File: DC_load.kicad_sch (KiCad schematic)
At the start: 21 parts, among them J2 4 mm terminal, J3 4 mm terminal, J4 4 mm terminal, J5 4 mm terminal, Q1 NPN, Q2 PNP, Q3 IRF3205, Q4 IRF3205, Q5 IRF3205, Q6 IRF3205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

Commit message: New dimensions.
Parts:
- removed D1, D2: 1N4148W, Diode_SMD:D_SOD-123, symbol Diode:1N4148W
- removed HS1: Heatsink, DC_load:AMD_heatsink, symbol Mechanical:Heatsink
- removed J3: 4 mm terminal, DC_load:4mm_terminal_red, symbol Connector:Screw_Terminal_01x01
- removed J4: 4 mm terminal, DC_load:4mm_terminal_black, symbol Connector:Screw_Terminal_01x01
- removed Q1: NPN, symbol Simulation_SPICE:NPN
- removed Q2: PNP, symbol Simulation_SPICE:PNP
- removed Q3, Q4, Q5, Q6: IRF3205, Package_TO_SOT_THT:TO-220-3_Horizontal_TabUp, symbol Transistor_FET:IRF3205
- added J1: Conn_Coaxial, Connector_Coaxial:BNC_Amphenol_B6252HB-NPP3G-50_Horizontal, symbol Connector:Conn_Coaxial
- added J6: USB_B, Connector_USB:USB_B_OST_USB-B1HSxx_Horizontal, symbol Connector:USB_B
- added U9: CH340C, Package_SO:SOIC-16_3.9x9.9mm_P1.27mm, symbol Interface_USB:CH340C
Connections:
- net GND: now also J1.2 (Ext), J6.4 (GND), J6.5 (Shield), U9.1 (GND)
- new net: J6.3 (D+), U9.5 (UD+)
- new net: J6.2 (D-), U9.6 (UD-)
- new net +5V: J6.1 (VBUS), U9.16 (VCC)
- new net BNC_CONTROL: J1.1 (In)
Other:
- added sheet Microcontroller (MCU.kicad_sch)
- added sheet Power_stage (power_stage.kicad_sch)
- moved on the sheet: J2, J5, U2

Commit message: Schematic progress.
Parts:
- removed J1: Conn_Coaxial, Connector_Coaxial:BNC_Amphenol_B6252HB-NPP3G-50_Horizontal, symbol Connector:Conn_Coaxial
- removed J2: 4 mm terminal, DC_load:4mm_terminal_red, symbol Connector:Screw_Terminal_01x01
- removed J5: 4 mm terminal, DC_load:4mm_terminal_black, symbol Connector:Screw_Terminal_01x01
- removed J6: USB_B, Connector_USB:USB_B_OST_USB-B1HSxx_Horizontal, symbol Connector:USB_B
- removed SW1, SW2: RotaryEncoder_Switch, DC_load:rotary_encoder_bottom_solder, symbol Device:RotaryEncoder_Switch
- removed U1: STM32F401RCTx, Package_QFP:LQFP-64_10x10mm_P0.5mm, symbol MCU_ST_STM32F4:STM32F401RCTx
- removed U2: Screen, PID_lib:WC1602A - below, symbol DC_load:2x16_screen
- removed U9: CH340C, Package_SO:SOIC-16_3.9x9.9mm_P1.27mm, symbol Interface_USB:CH340C

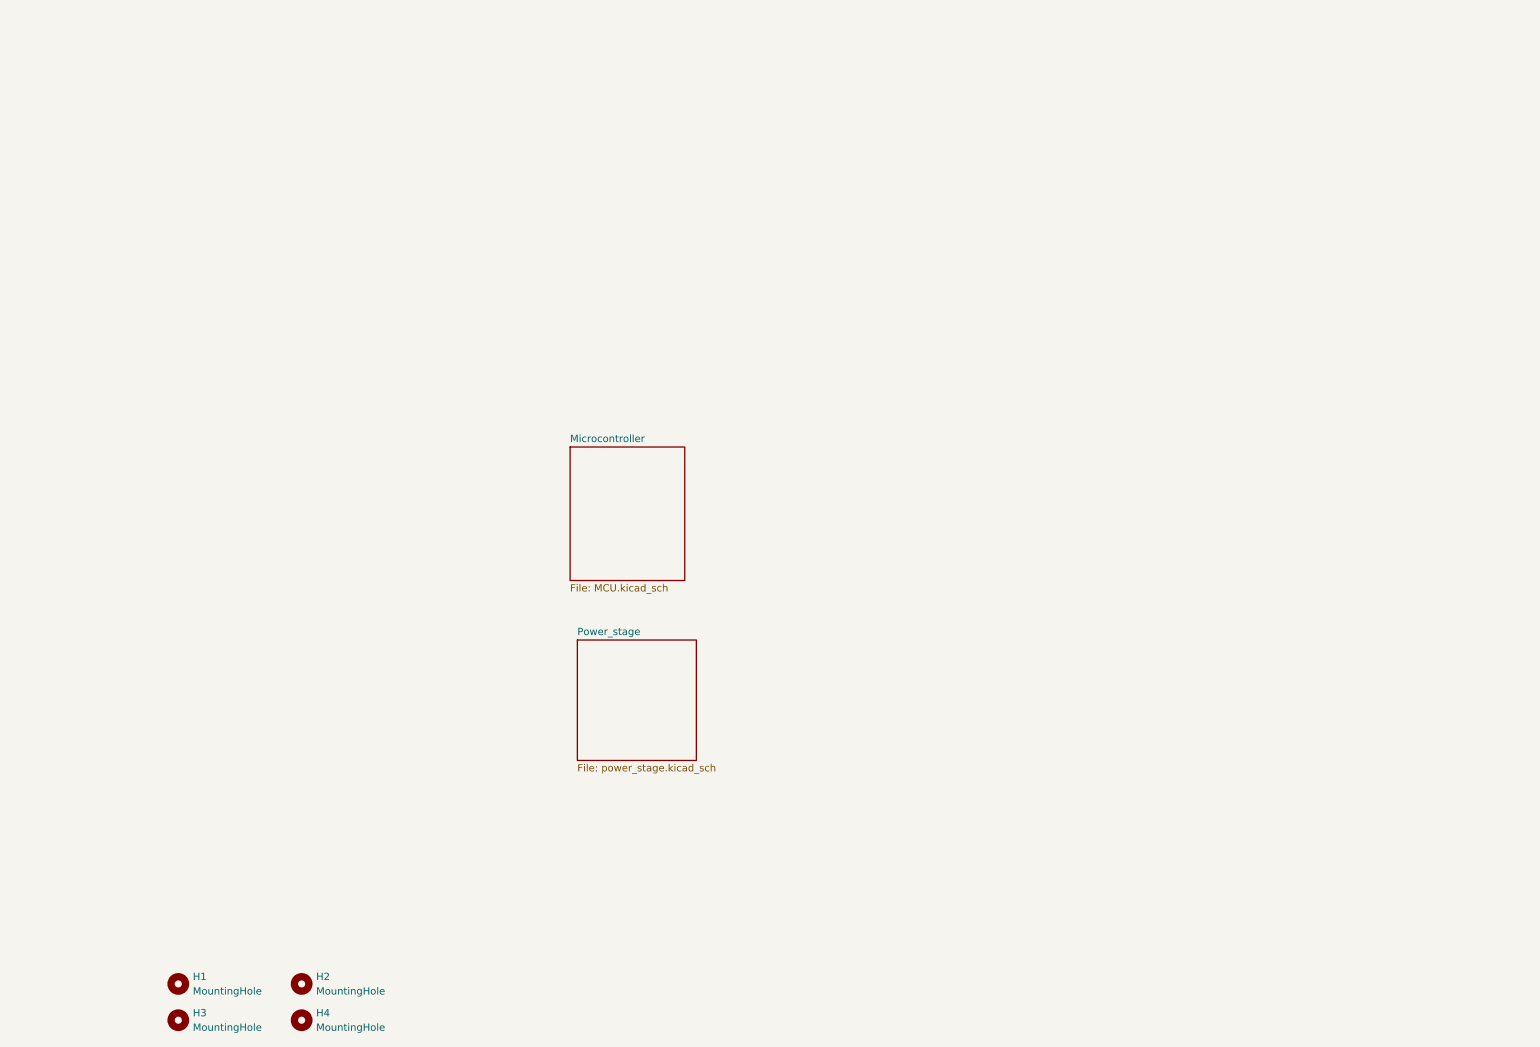
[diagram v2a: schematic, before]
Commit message: Schematic and placement update.
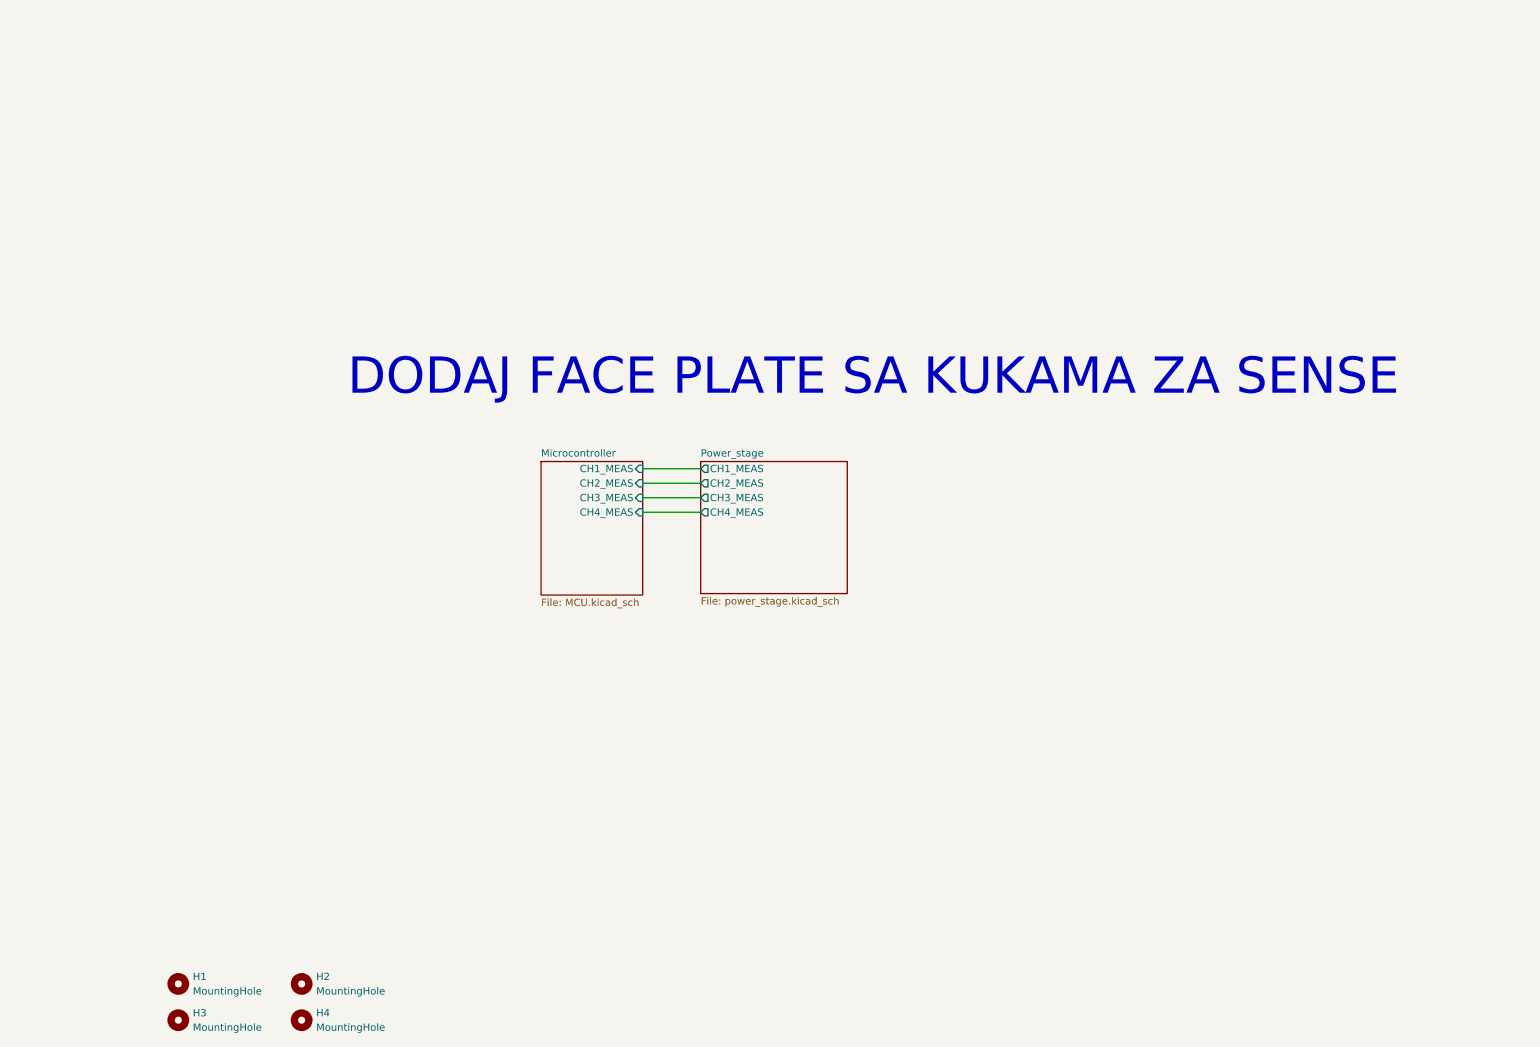
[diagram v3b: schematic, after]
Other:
- sheet Microcontroller ports: added CH1_MEAS, CH2_MEAS, CH3_MEAS, CH4_MEAS; removed none
- sheet Power_stage ports: added CH1_MEAS, CH2_MEAS, CH3_MEAS, CH4_MEAS; removed none
- note added: "DODAJ FACE PLATE SA KUKAMA ZA SENSE"
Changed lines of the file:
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@@
 	(generator_version "9.0")
 	(paper "A4")
+	(text "DODAJ FACE PLATE SA KUKAMA ZA SENSE"
+		(exclude_from_sim no)
+		(at 164.846 80.518 0)
+		(effects
+			(font
+				(size 6.35 6.35)
+			)
+		)
+	)
+	(wire
+		(pts
+			(xy 124.46 99.06) (xy 134.62 99.06)
+		)
+		(stroke
+			(width 0)
+			(type default)
+		)
+	)
+	(wire
+		(pts
+			(xy 124.46 101.6) (xy 134.62 101.6)
+		)
+		(stroke
+			(width 0)
+			(type default)
+		)
+	)
+	(wire
+		(pts
+			(xy 124.46 104.14) (xy 134.62 104.14)
+		)
+		(stroke
+			(width 0)
+			(type default)
+		)
+	)
+	(wire
+		(pts
+			(xy 124.46 96.52) (xy 134.62 96.52)
+		)
+		(stroke
+			(width 0)
+			(type default)
+		)
+	)
 	(symbol
 		(lib_id "Mechanical:MountingHole")
@@
 	)
 	(sheet
-		(at 111.76 92.71)
-		(size 20.066 23.368)
+		(at 106.68 95.25)
+		(size 17.78 23.368)
 		(exclude_from_sim no)
 		(in_bom yes)
@@
 		)
 		(property "Sheetname" "Microcontroller"
-			(at 111.76 91.9984 0)
+			(at 106.68 94.5384 0)
 			(effects
 				(font
@@
 		)
 		(property "Sheetfile" "MCU.kicad_sch"
-			(at 111.76 116.6626 0)
+			(at 106.68 119.2026 0)
 			(effects
 				(font
@@
 				)
 				(justify left top)
+			)
+		)
+		(pin "CH1_MEAS" input
+			(at 124.46 96.52 0)
+			(effects
+				(font
+					(size 1.27 1.27)
+				)
+				(justify right)
+			)
+		)
+		(pin "CH4_MEAS" input
+			(at 124.46 104.14 0)
+			(effects
+				(font
+					(size 1.27 1.27)
+				)
+				(justify right)
+			)
+		)
+		(pin "CH2_MEAS" input
+			(at 124.46 99.06 0)
+			(effects
+				(font
+					(size 1.27 1.27)
+				)
+				(justify right)
+			)
+		)
+		(pin "CH3_MEAS" input
+			(at 124.46 101.6 0)
+			(effects
+				(font
+					(size 1.27 1.27)
+				)
+				(justify right)
 			)
 		)
@@
 	)
 	(sheet
-		(at 113.03 126.492)
-		(size 20.828 21.082)
+		(at 134.62 95.25)
+		(size 25.654 23.114)
 		(exclude_from_sim no)
 		(in_bom yes)
@@
 		)
 		(property "Sheetname" "Power_stage"
-			(at 113.03 125.7804 0)
+			(at 134.62 94.5384 0)
 			(effects
 				(font
@@
 		)
 		(property "Sheetfile" "power_stage.kicad_sch"
-			(at 113.03 148.1586 0)
+			(at 134.62 118.9486 0)
 			(effects
 				(font
@@
 			)
 		)
+		(pin "CH4_MEAS" output
+			(at 134.62 104.14 180)
+			(effects
+				(font
+					(size 1.27 1.27)
+				)
+				(justify left)
+			)
+		)
+		(pin "CH1_MEAS" output
+			(at 134.62 96.52 180)
+			(effects
+				(font
+					(size 1.27 1.27)
+				)
+				(justify left)
+			)
+		)
+		(pin "CH3_MEAS" output
+			(at 134.62 101.6 180)
+			(effects
+				(font
+					(size 1.27 1.27)
+				)
+				(justify left)
+			)
+		)
+		(pin "CH2_MEAS" output
+			(at 134.62 99.06 180)
+			(effects
+				(font
+					(size 1.27 1.27)
+				)
+				(justify left)
+			)
+		)
